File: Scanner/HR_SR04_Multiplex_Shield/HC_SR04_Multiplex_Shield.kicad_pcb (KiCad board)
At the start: 2 copper layers, 68.6 x 53.3 mm, 21 parts, among them J1 Conn_01x02, J10 Conn_01x02, J11 Conn_01x02, J2 Conn_01x02, J3 Conn_01x02, J4 Conn_01x02, J5 Conn_01x02, J6 Conn_01x02, J7 Conn_01x02, J8 Conn_01x02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

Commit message: exported topor autoroute, still needs some work
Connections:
- P3 pad 1: /A5(SCL) -> /A5
- P3 pad 2: /A4(SDA) -> /A4
- P3 pad 6: /12(MISO) -> /12
- P4 pad 3: /5(**) -> /5
- P4 pad 5: /3(**) -> /3
- U1 pad 10: /6 -> /2
- U1 pad 11: /7 -> /3
- U1 pad 13: /9 -> /5
- U1 pad 14: /8 -> /4

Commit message: routed and ready for manufacture
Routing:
- net /2: track 0.00 -> 89.0 mm
- net GND: track 0.00 -> 86.1 mm, vias 0 -> 1
- net /3: track 0.00 -> 58.1 mm
- net /A0: track 0.00 -> 57.5 mm
- net /4: track 0.00 -> 54.2 mm, vias 0 -> 1
- net /5: track 0.00 -> 53.7 mm, vias 0 -> 1
- net +5V: track 0.00 -> 53.0 mm
- net /E8: track 0.00 -> 48.6 mm
- net /T4: track 0.00 -> 46.4 mm
- net /T8: track 0.00 -> 46.4 mm
- net /T9: track 0.00 -> 46.0 mm
- net /10(ECHO): track 0.00 -> 44.6 mm
- net /T7: track 0.00 -> 43.1 mm
- net /T6: track 0.00 -> 40.6 mm
- net /E11: track 0.00 -> 36.0 mm
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- added copper zone on F.Cu, net GND
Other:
- net class Default: clearance 0.2 -> 0.1524
- rule trace_clearance: 0.2 -> 0.1524

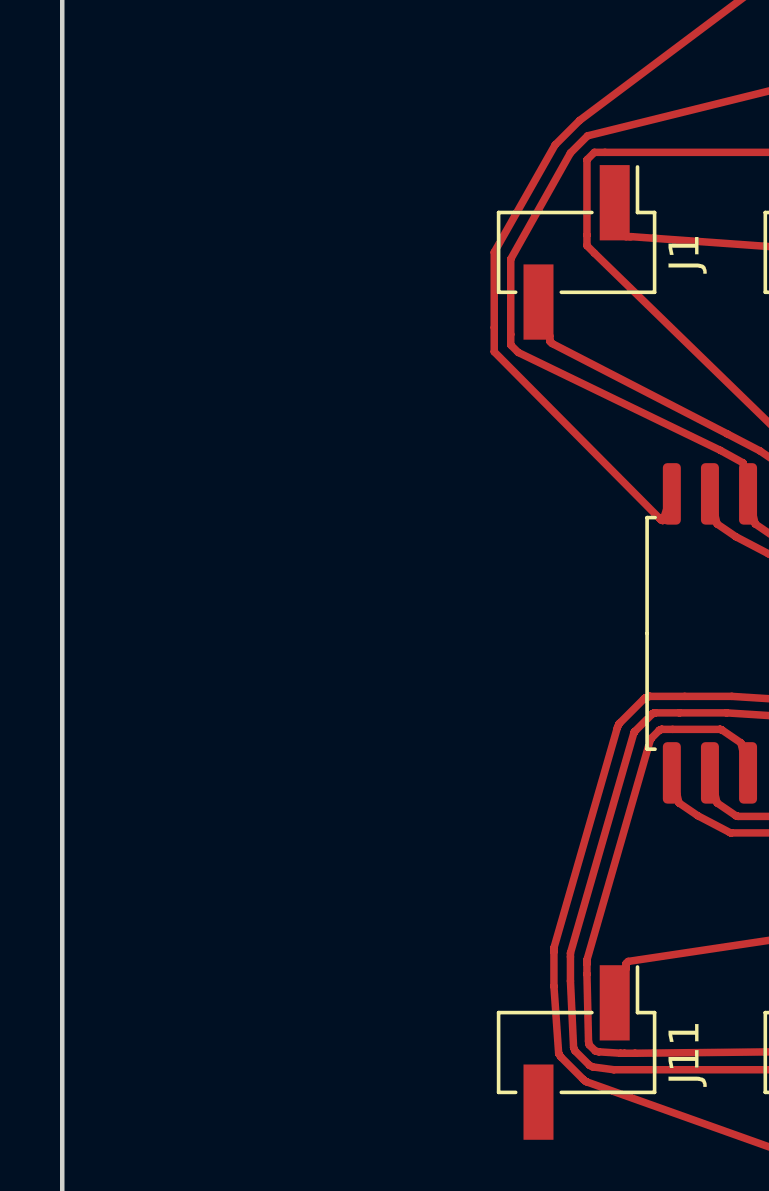
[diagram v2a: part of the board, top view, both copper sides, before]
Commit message: added "SpookyAlexa" silk text
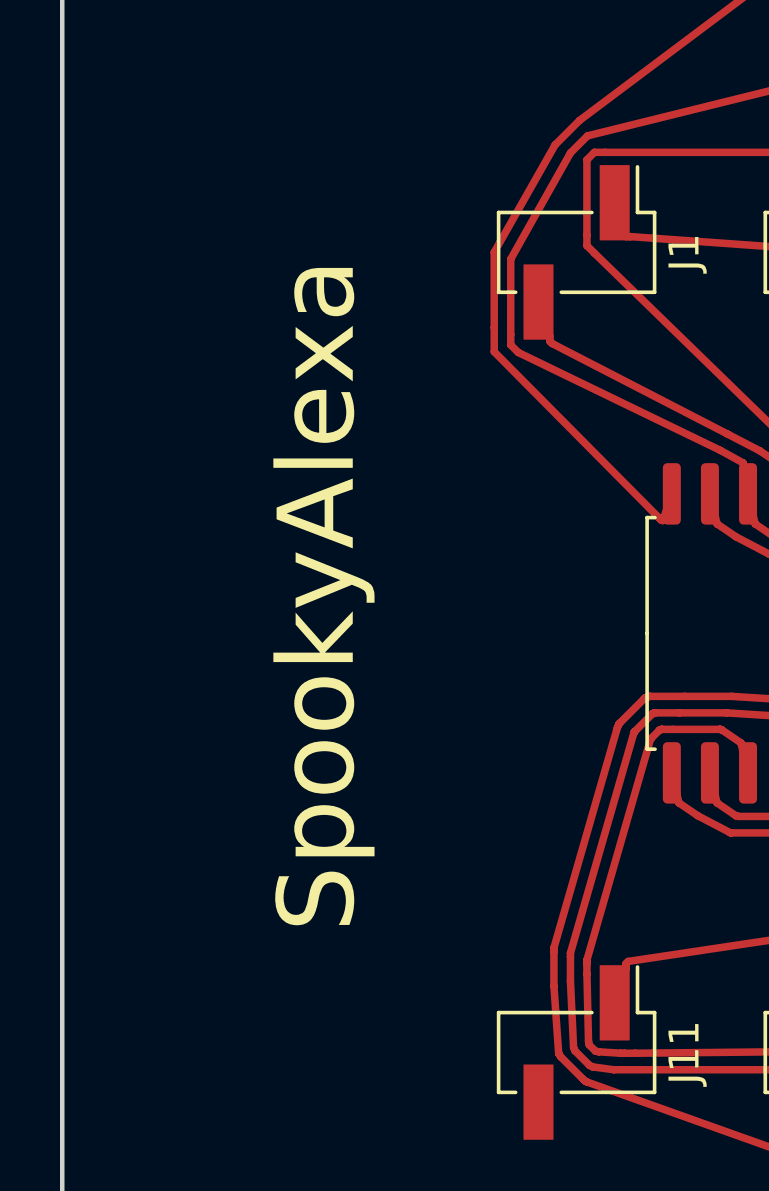
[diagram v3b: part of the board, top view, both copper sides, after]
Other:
- board text added: "SpookyAlexa"
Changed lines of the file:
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@@
   (general
     (thickness 1.6)
-    (drawings 27)
+    (drawings 28)
     (tracks 666)
     (zones 0)
@@
     )
   )
+  (gr_text SpookyAlexa (at 119.507 98.425 90) (layer F.SilkS)
+    (effects (font (size 2.54 2.54) (thickness 0.3)))
+  )
   (gr_text 1 (at 138.938 121.285 90) (layer F.SilkS)

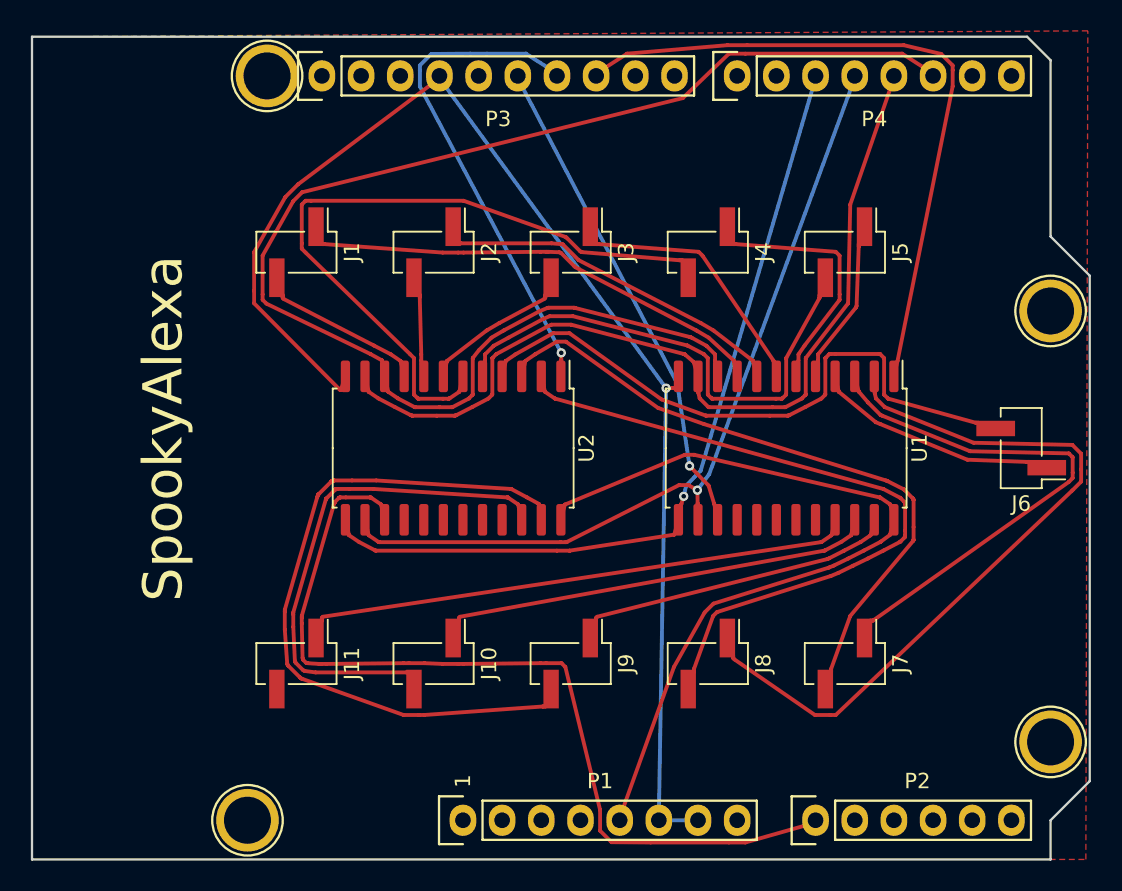
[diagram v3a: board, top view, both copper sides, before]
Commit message: removed ground plane bcuz it looks cooler
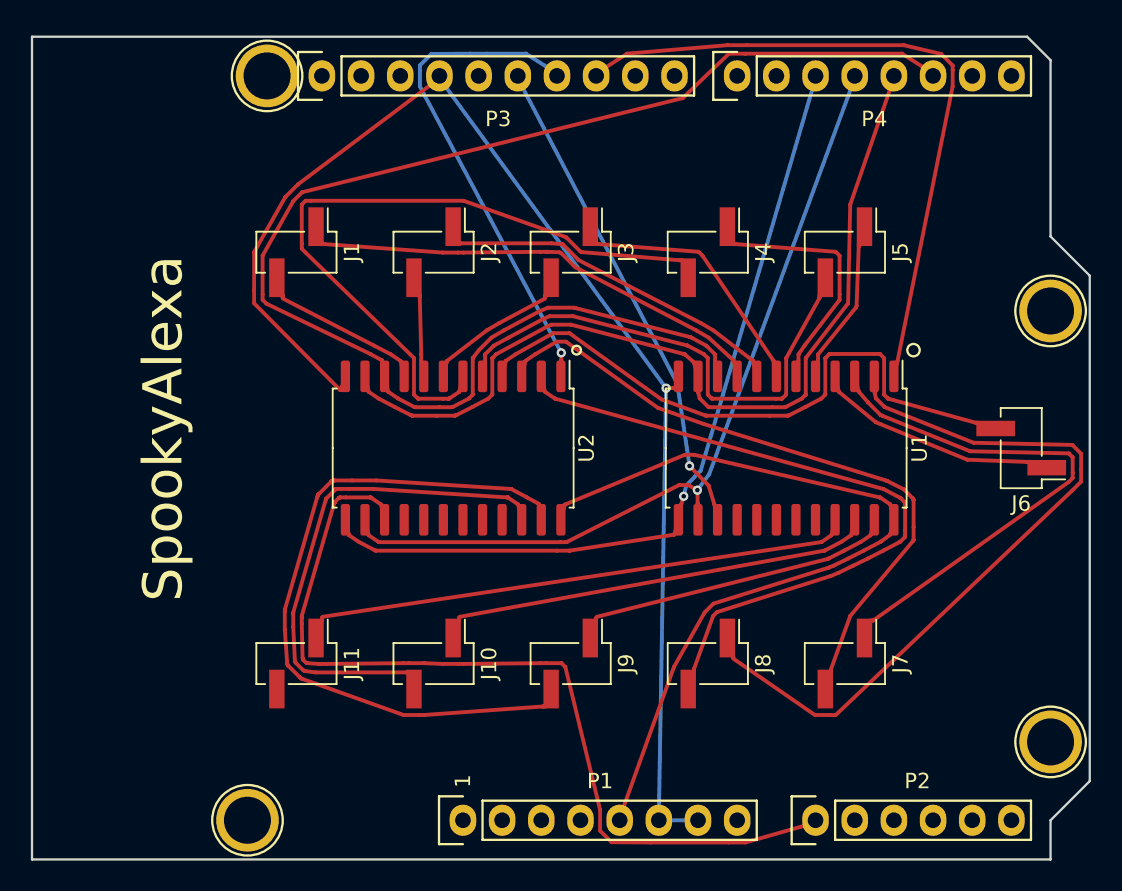
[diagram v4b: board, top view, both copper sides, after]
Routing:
- removed copper zone on F.Cu, net GND
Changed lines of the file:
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@@
   (general
     (thickness 1.6)
-    (drawings 28)
+    (drawings 30)
     (tracks 666)
     (zones 0)
@@
     )
   )
+  (gr_circle (center 146.304 93.345) (end 146.558 93.472) (layer F.SilkS) (width 0.15))
+  (gr_circle (center 168.148 93.345) (end 168.275 93.726) (layer F.SilkS) (width 0.15))
   (gr_text SpookyAlexa (at 119.507 98.425 90) (layer F.SilkS)
     (effects (font (size 2.54 2.54) (thickness 0.3)))
@@
   (segment (start 164.0479 83.9089) (end 166.878 75.7174) (width 0.25) (layer F.Cu) (net 65))
   (segment (start 166.878 75.7174) (end 166.878 75.565) (width 0.25) (layer F.Cu) (net 65))
-  (zone (net 4) (net_name GND) (layer F.Cu) (hatch edge 0.508)
-    (connect_pads (clearance 0.508))
-    (min_thickness 0.254)
-    (fill yes (arc_segments 32) (thermal_gap 0.508) (thermal_bridge_width 0.508))
-    (polygon
-      (pts
-        (xy 110.998 73.025) (xy 110.998 126.365) (xy 179.324 126.365) (xy 179.451 72.644)
-      )
-    )
-  )
 )
